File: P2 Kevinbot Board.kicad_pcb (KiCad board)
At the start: 4 copper layers, 156.5 x 85.4 mm, 56 parts, among them J1 Conn_01x03_Pin, J10 Conn_02x04_Counter_Clockwise, J12 Conn_02x06_Odd_Even, J16 Conn_02x06_Odd_Even, J2 Conn_01x03_Pin, J3 USB_C_Receptacle_USB2.0_16P, J4 Conn_01x02_Pin, J5 Conn_01x02_Pin, J6 Conn_02x06_Odd_Even, J7 Conn_01x02_Pin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

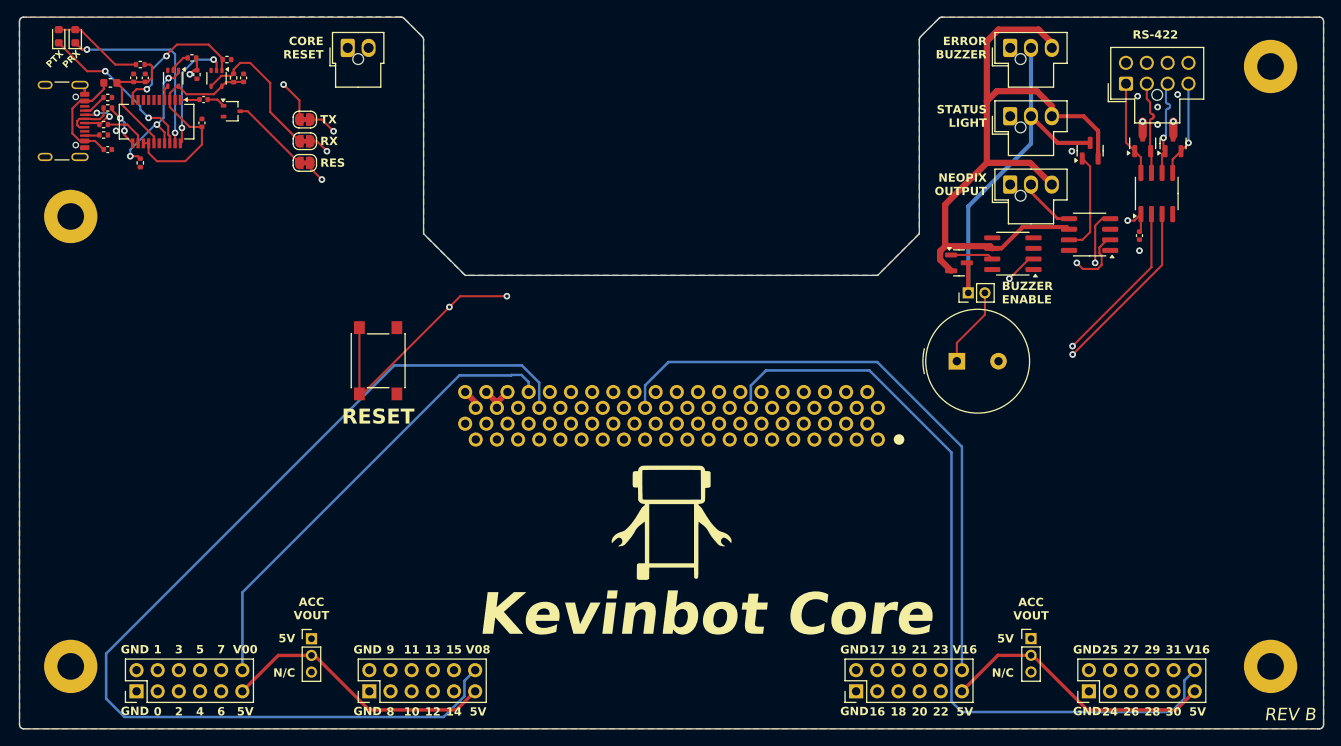
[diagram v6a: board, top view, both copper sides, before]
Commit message: rs422, pcb: uart/rs422 mux
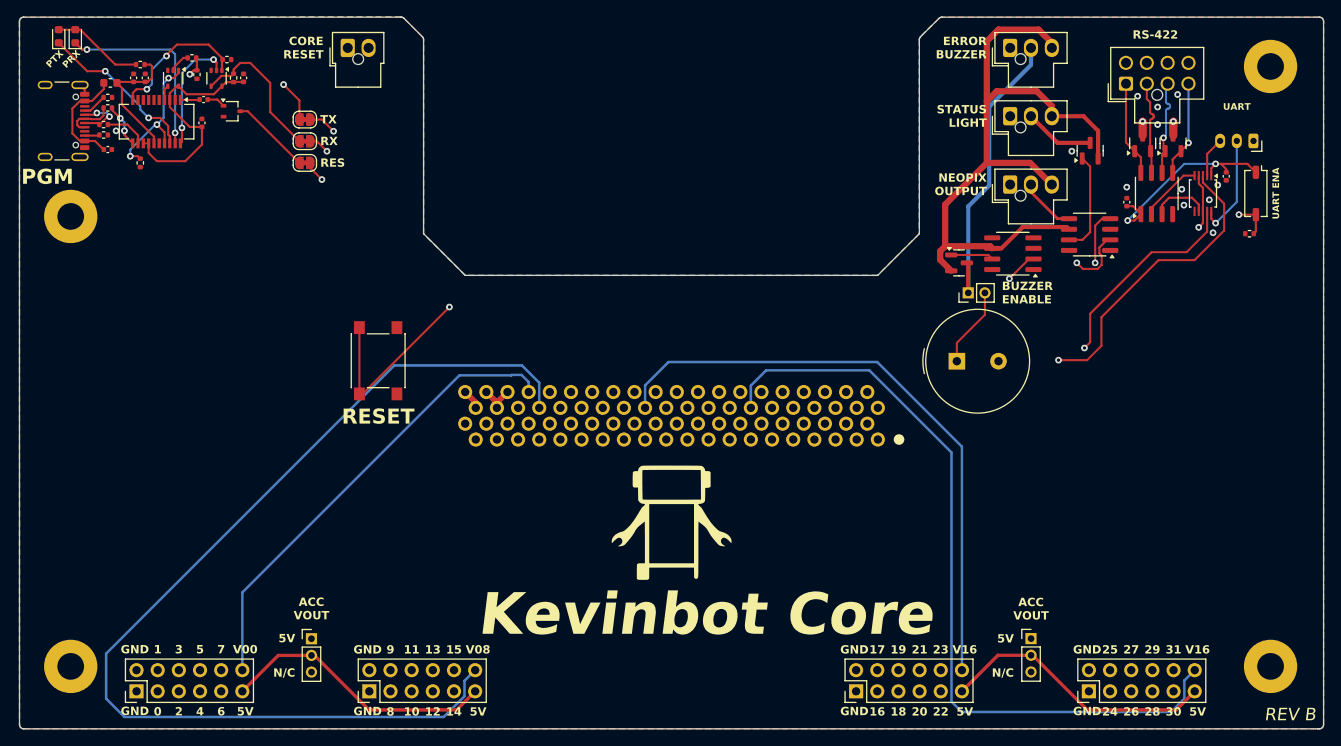
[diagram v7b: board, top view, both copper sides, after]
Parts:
- added C8: 100nF, Capacitor_SMD:C_0402_1005Metric, F.Cu at (230.8, 74.3)
- added J11: Conn_01x03_Pin, Connector_JST:JST_PH_B3B-PH-K_1x03_P2.00mm_Vertical, F.Cu at (234.0, 70.0)
- added R11: 10k, Resistor_SMD:R_0402_1005Metric, F.Cu at (233.6, 81.2)
- added SW2: SW_DIP_x01, Button_Switch_SMD:SW_DIP_SPSTx01_Slide_Copal_CHS-01A_W5.08mm_P1.27mm_JPin, F.Cu at (234.3, 76.3)
- added U8: TS3A24159DGS, Package_SO:TSSOP-10_3x3mm_P0.5mm, F.Cu at (228.0, 76.3)
- moved C7 4.29 mm to (218.8, 77.4), turned to -90 degrees
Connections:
- U5 pad 2: P2_P36 -> /RS-422/RX_422
- U5 pad 3: P2_P35 -> /RS-422/TX_422
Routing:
- net P2_V32: track 48.5 -> 70.0 mm, vias 1 -> 2
- net /RS-422/EN_UART: track 0.00 -> 16.5 mm, vias 0 -> 2
- net P2_P36: track 55.8 -> 69.6 mm
- net /RS-422/TX_UART: track 0.00 -> 12.5 mm, vias 0 -> 1
- net /RS-422/RX_422: track 0.00 -> 7.54 mm
- net /P2_RESn: track 88.9 -> 81.4 mm, vias 3 -> 2
- net /RS-422/TX_422: track 0.00 -> 7.04 mm
- net P2_P35: track 56.5 -> 61.8 mm
- net /RS-422/RX_UART: track 0.00 -> 4.81 mm
- net GND: vias 9 -> 14
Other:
- board text added: "PGM"
- board text added: "UART"
- board text added: "UART ENA"

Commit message: docs: add wire info, psu: add connector, i2c: initial work, lots of changes
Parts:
- added C9: 100nF, Capacitor_SMD:C_0402_1005Metric, F.Cu at (215.8, 90.7)
- added J13: Conn_02x02_Odd_Even, Connector_Molex:Molex_Micro-Fit_3.0_43045-0400_2x02_P3.00mm_Horizontal, F.Cu at (95.3, 94.1)
- added J14: Conn_02x03_Top_Bottom, Connector_Molex:Molex_Nano-Fit_105310-xx06_2x03_P2.50mm_Vertical, F.Cu at (220.0, 88.8)
- added JP5: SolderJumper_2_Bridged, Jumper:SolderJumper-2_P1.3mm_Bridged_RoundedPad1.0x1.5mm, F.Cu at (210.8, 95.8)
- added U9: LTC4311, Package_TO_SOT_SMD:SOT-363_SC-70-6, F.Cu at (215.8, 92.7)
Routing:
- net P2_P42: track 0.00 -> 50.2 mm, vias 0 -> 1
- net P2_P41: track 0.00 -> 48.9 mm, vias 0 -> 1
- net P2_V40: track 0.00 -> 46.3 mm
- net Net-(JP5-B): track 0.00 -> 5.88 mm
- net P2_P36: track 69.6 -> 67.6 mm
- net P2_P35: track 61.8 -> 63.7 mm
- net GND: vias 14 -> 16
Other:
- board text added: "I2C"
- board text added: "I2C ACCEL ENA"
- board text added: "POWER 6~40V"
